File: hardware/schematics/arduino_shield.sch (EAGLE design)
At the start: 41 parts, among them IC1 LM358KIT, IC2 MAX548, Q1 IRL520N-H, Q2 IRL520N-H, Q3 IRF9Z24, Q4 IRL520N-H, Q5 IRL520N-H, Q6 IRF9Z24, X5 Channel A, X6 Channel B

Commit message: update
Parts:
- removed X5: Channel A, adafruit:STEREOJACK
- removed X6: Channel B, adafruit:STEREOJACK
- added CHANNELA, CHANNELB: (no value), SparkFun-Connectors:AUDIO-JACK2.5MM
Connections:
- net N$1: now also CHANNELA.SLEEVE, TR1.6; no longer TR1.4, X5.1
- net N$2: now also CHANNELB.SLEEVE, TR2.6; no longer TR1.6, X5.2, X5.5
- net N$3: now also CHANNELB.LEFT, CHANNELB.RIGHT, TR2.4; no longer TR2.6, X6.2, X6.5
- net N$4: now also CHANNELA.LEFT, CHANNELA.RIGHT, TR1.4; no longer TR2.4, X6.1
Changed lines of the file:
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@@
 <?xml version="1.0" encoding="utf-8"?>
 <!DOCTYPE eagle SYSTEM "eagle.dtd">
-<eagle version="7.1.0">
+<eagle version="7.3.0">
 <drawing>
 <settings>
@@
 <part name="GND15" library="supply1" deviceset="GND" device=""/>
 <part name="R22" library="eagle-ltspice" deviceset="R" device="" value="100k"/>
-<part name="X5" library="adafruit" deviceset="STEREOJACK" device="" value="Channel A"/>
-<part name="X6" library="adafruit" deviceset="STEREOJACK" device="" value="Channel B"/>
 <part name="GND21" library="supply1" deviceset="GND" device=""/>
 <part name="U$3" library="adafruit" deviceset="ARDUINO" device="UNO"/>
@@
 <part name="JP2" library="SparkFun-Connectors" deviceset="M02" device="3.5MM"/>
 <part name="GND4" library="supply1" deviceset="GND" device=""/>
+<part name="CHANNELA" library="SparkFun-Connectors" deviceset="AUDIO-JACK" device="2.5MM"/>
+<part name="CHANNELB" library="SparkFun-Connectors" deviceset="AUDIO-JACK" device="2.5MM"/>
 </parts>
 <sheets>
@@
 <instance part="R22" gate="G$1" x="66.04" y="55.88"/>
 <instance part="FRAME6" gate="G$1" x="0" y="0"/>
-<instance part="X5" gate="1" x="215.9" y="149.86"/>
-<instance part="X6" gate="1" x="215.9" y="68.58"/>
 <instance part="GND21" gate="1" x="134.62" y="10.16"/>
 <instance part="P+7" gate="1" x="88.9" y="86.36"/>
@@
 <instance part="P+10" gate="1" x="50.8" y="111.76"/>
 <instance part="GND3" gate="1" x="15.24" y="86.36"/>
+<instance part="CHANNELA" gate="G$1" x="215.9" y="149.86" rot="MR0"/>
+<instance part="CHANNELB" gate="G$1" x="215.9" y="68.58" rot="MR0"/>
 </instances>
 <busses>
@@
 <wire x1="132.08" y1="48.26" x2="132.08" y2="45.72" width="0.1524" layer="91"/>
 <junction x="132.08" y="45.72"/>
-</segment>
-</net>
-<net name="N$1" class="0">
-<segment>
-<pinref part="TR1" gate="G$1" pin="4"/>
-<pinref part="X5" gate="1" pin="1"/>
-<wire x1="195.58" y1="142.24" x2="203.2" y2="142.24" width="0.1524" layer="91"/>
-</segment>
-</net>
-<net name="N$2" class="0">
-<segment>
-<pinref part="TR1" gate="G$1" pin="6"/>
-<pinref part="X5" gate="1" pin="5"/>
-<wire x1="195.58" y1="152.4" x2="200.66" y2="152.4" width="0.1524" layer="91"/>
-<wire x1="203.2" y1="152.4" x2="200.66" y2="152.4" width="0.1524" layer="91"/>
-<wire x1="200.66" y1="152.4" x2="200.66" y2="144.78" width="0.1524" layer="91"/>
-<pinref part="X5" gate="1" pin="2"/>
-<wire x1="200.66" y1="144.78" x2="203.2" y2="144.78" width="0.1524" layer="91"/>
-<junction x="200.66" y="152.4"/>
-</segment>
-</net>
-<net name="N$3" class="0">
-<segment>
-<pinref part="TR2" gate="G$1" pin="6"/>
-<pinref part="X6" gate="1" pin="5"/>
-<wire x1="195.58" y1="71.12" x2="200.66" y2="71.12" width="0.1524" layer="91"/>
-<wire x1="203.2" y1="71.12" x2="200.66" y2="71.12" width="0.1524" layer="91"/>
-<wire x1="200.66" y1="71.12" x2="200.66" y2="63.5" width="0.1524" layer="91"/>
-<pinref part="X6" gate="1" pin="2"/>
-<wire x1="200.66" y1="63.5" x2="203.2" y2="63.5" width="0.1524" layer="91"/>
-<junction x="200.66" y="71.12"/>
-</segment>
-</net>
-<net name="N$4" class="0">
-<segment>
-<pinref part="X6" gate="1" pin="1"/>
-<pinref part="TR2" gate="G$1" pin="4"/>
-<wire x1="203.2" y1="60.96" x2="195.58" y2="60.96" width="0.1524" layer="91"/>
 </segment>
 </net>
@@
 </segment>
 </net>
+<net name="N$1" class="0">
+<segment>
+<pinref part="CHANNELA" gate="G$1" pin="SLEEVE"/>
+<pinref part="TR1" gate="G$1" pin="6"/>
+<wire x1="210.82" y1="152.4" x2="195.58" y2="152.4" width="0.1524" layer="91"/>
+</segment>
+</net>
+<net name="N$2" class="0">
+<segment>
+<pinref part="CHANNELB" gate="G$1" pin="SLEEVE"/>
+<pinref part="TR2" gate="G$1" pin="6"/>
+<wire x1="210.82" y1="71.12" x2="195.58" y2="71.12" width="0.1524" layer="91"/>
+</segment>
+</net>
+<net name="N$3" class="0">
+<segment>
+<pinref part="CHANNELB" gate="G$1" pin="RIGHT"/>
+<wire x1="210.82" y1="68.58" x2="203.2" y2="68.58" width="0.1524" layer="91"/>
+<wire x1="203.2" y1="68.58" x2="203.2" y2="66.04" width="0.1524" layer="91"/>
+<pinref part="TR2" gate="G$1" pin="4"/>
+<wire x1="203.2" y1="66.04" x2="203.2" y2="60.96" width="0.1524" layer="91"/>
+<wire x1="203.2" y1="60.96" x2="195.58" y2="60.96" width="0.1524" layer="91"/>
+<pinref part="CHANNELB" gate="G$1" pin="LEFT"/>
+<wire x1="210.82" y1="66.04" x2="203.2" y2="66.04" width="0.1524" layer="91"/>
+<junction x="203.2" y="66.04"/>
+</segment>
+</net>
+<net name="N$4" class="0">
+<segment>
+<pinref part="CHANNELA" gate="G$1" pin="RIGHT"/>
+<wire x1="210.82" y1="149.86" x2="203.2" y2="149.86" width="0.1524" layer="91"/>
+<wire x1="203.2" y1="149.86" x2="203.2" y2="147.32" width="0.1524" layer="91"/>
+<pinref part="TR1" gate="G$1" pin="4"/>
+<wire x1="203.2" y1="147.32" x2="203.2" y2="142.24" width="0.1524" layer="91"/>
+<wire x1="203.2" y1="142.24" x2="195.58" y2="142.24" width="0.1524" layer="91"/>
+<pinref part="CHANNELA" gate="G$1" pin="LEFT"/>
+<wire x1="210.82" y1="147.32" x2="203.2" y2="147.32" width="0.1524" layer="91"/>
+<junction x="203.2" y="147.32"/>
+</segment>
+</net>

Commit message: schematics
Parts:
- removed JP1: (no value), jumper:JP2E
- removed JP2: M023.5MM, SparkFun-Connectors:M023.5MM
- Q2, Q5: value IRL520N-H -> IRF9Z24
- Q3, Q6: value IRF9Z24 -> IRL520N-H
- renumbered C4 to C2, U$3 to GND
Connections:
- removed net N$7: GND.VIN, JP1.3
- removed net N$8: JP1.1, JP2.1
- net +12V: now also GND.VIN, Q2.S, Q5.S; no longer JP1.2, Q3.S, Q6.S
- net ADC1: now also Q3.S, Q6.S; no longer Q2.S, Q5.S
- net GND: no longer JP2.2
- net N$19: now also Q3.G; no longer Q2.G
- net N$21: now also Q2.G; no longer Q3.G
- net N$25: now also Q6.G; no longer Q5.G
- net N$27: now also Q5.G; no longer Q6.G
- net N$35: now also Q2.D; no longer Q3.D
- net N$37: now also Q5.D; no longer Q6.D
- net N$38: now also Q6.D; no longer Q5.D
- net N$39: now also Q3.D; no longer Q2.D

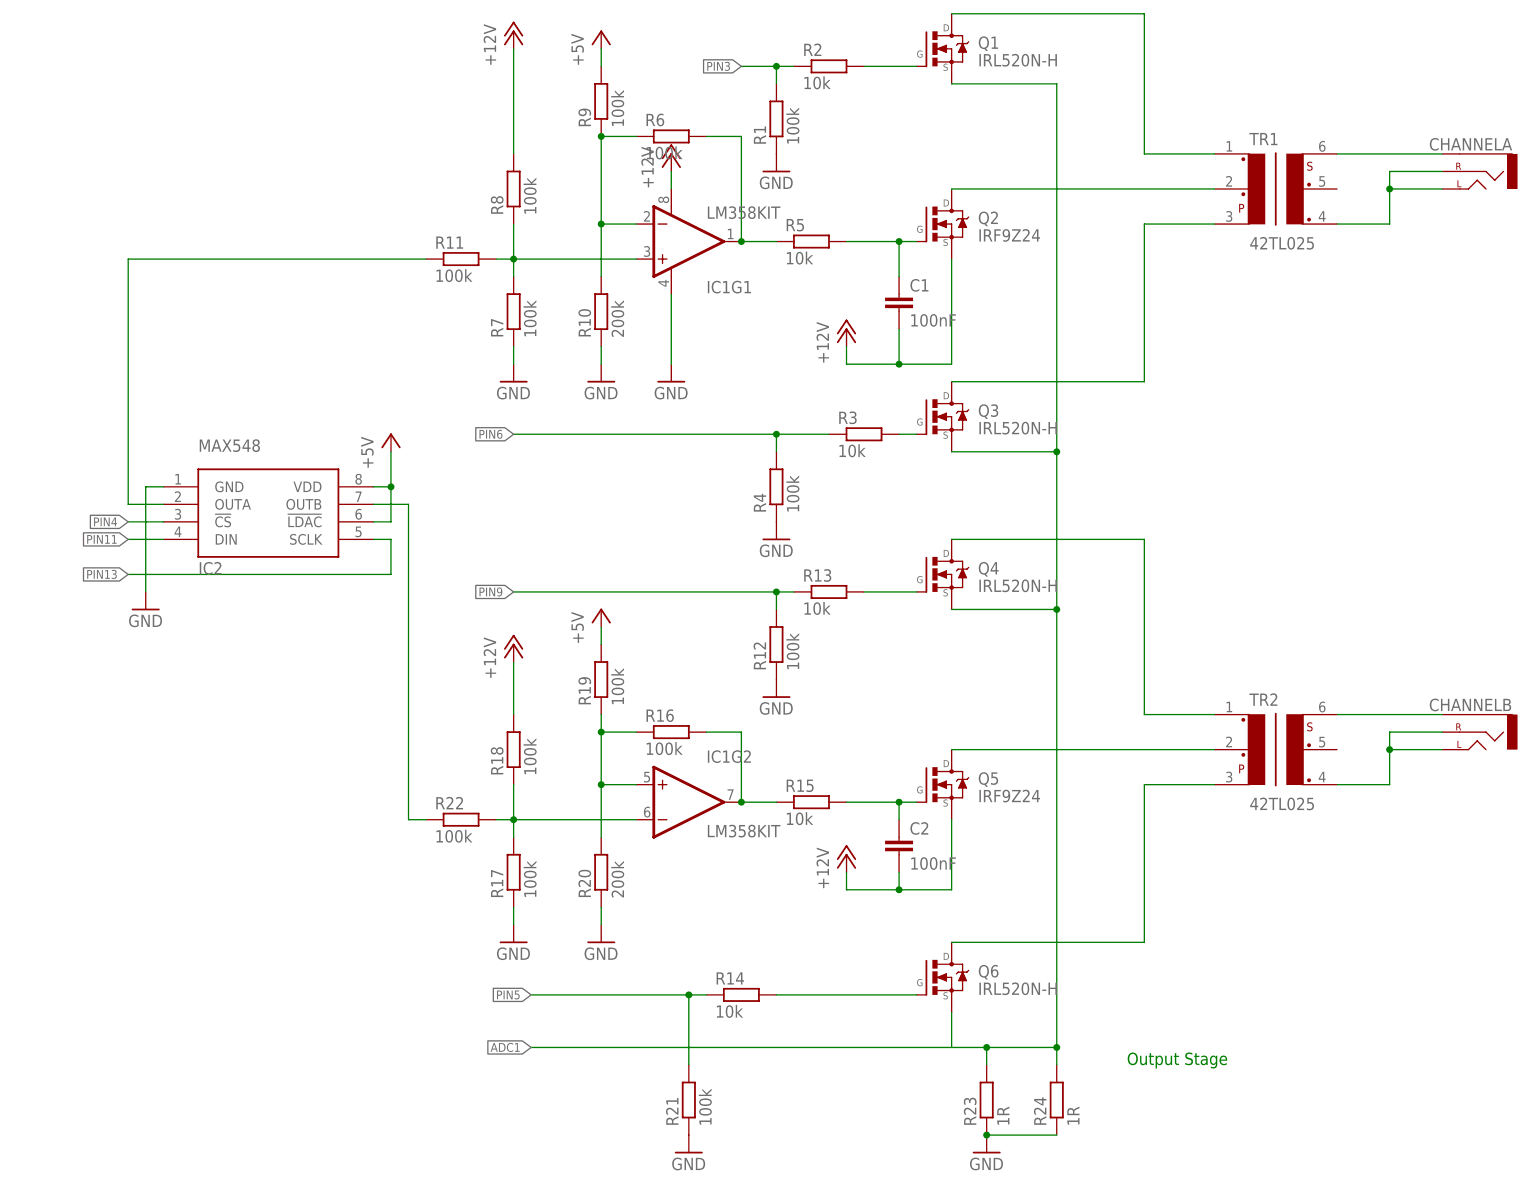
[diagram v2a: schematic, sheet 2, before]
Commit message: Changes by FluffyBit
done:

- changed grid to 0.1mm to help place components
- forced all components onto 0.1mm grid
- added gnd plane on bottom of board
- added two caps for decoupling the DAC+OP-AMP
- added 10K pull-up on the nCS line to the DAC

ideas:
- add LED on unused digital pin.

fixes
- IC1G2 swaped +/- input to make negative feedback

notes:

no decoupling on +5V (fixed)

no bulk decoupling on +12V or +5V
-> suggest 10uF 0805 on 5V near DAC
-> suggest 10uF near op-amp area
-> suggest 47uF or 100uF near the +12V transformer drive

bias for op-amps seem to be either 5V or 12V (not consistent)

if digital-io is not important then you could:
- 5->8
- 3->7

todo:
- check body-diode on pfets driving transformer centre-tap
 -> think it is ok, diode goes drain-to-source on selected FET
 -> source is the outer pin (drain middle)
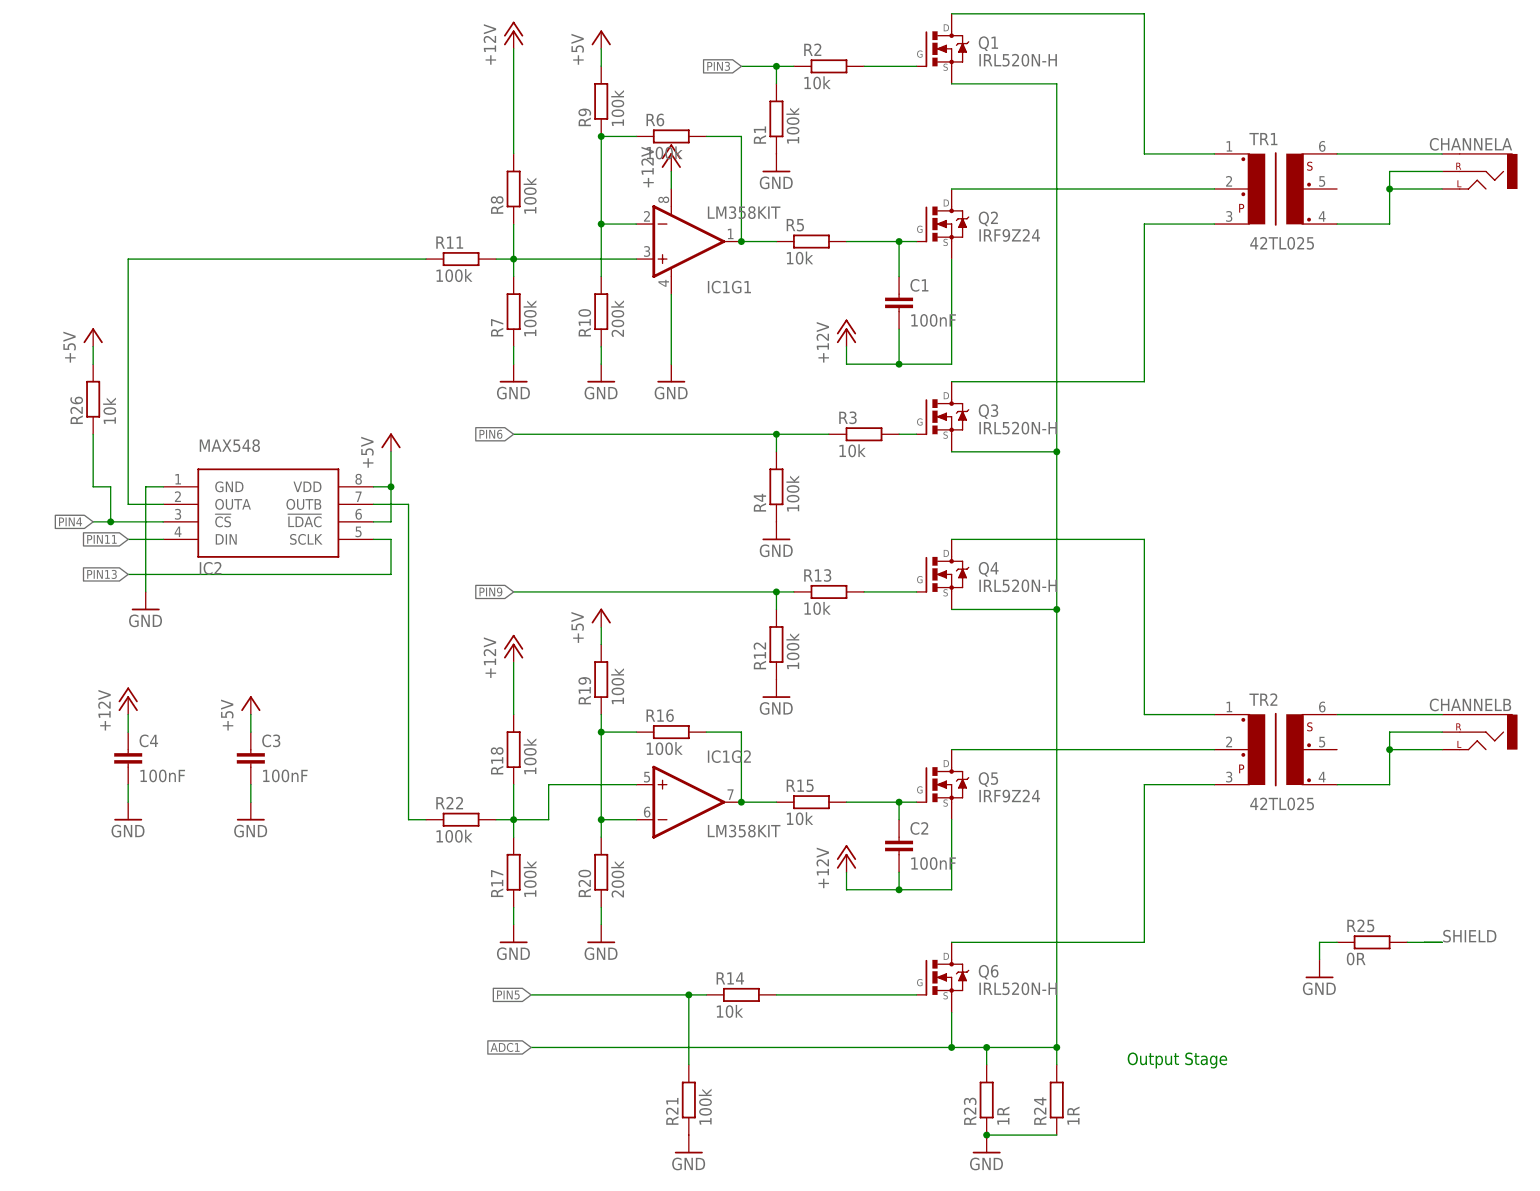
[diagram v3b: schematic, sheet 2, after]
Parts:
- added C3, C4: 100nF, capacitor-wima:C2.5/2
- added R25: 0R, eagle-ltspice:R
- added R26: 10k, eagle-ltspice:R
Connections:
- new net SHIELD: R25.2
- net +12V: now also C4.1
- net +5V: now also C3.1, R26.2
- net GND: now also C3.2, C4.2, R25.1
- net N$28: now also IC1G2.+IN; no longer IC1G2.-IN
- net N$41: now also IC1G2.-IN; no longer IC1G2.+IN
- net PIN4: now also R26.1
